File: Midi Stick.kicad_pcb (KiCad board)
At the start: 2 copper layers, 47.1 x 17.5 mm, 34 parts, among them J1 USB 2.0 Type A Plug, J2 Aux, J3 ICSP, Q1 Mosfet N, X1 X1E0000210019

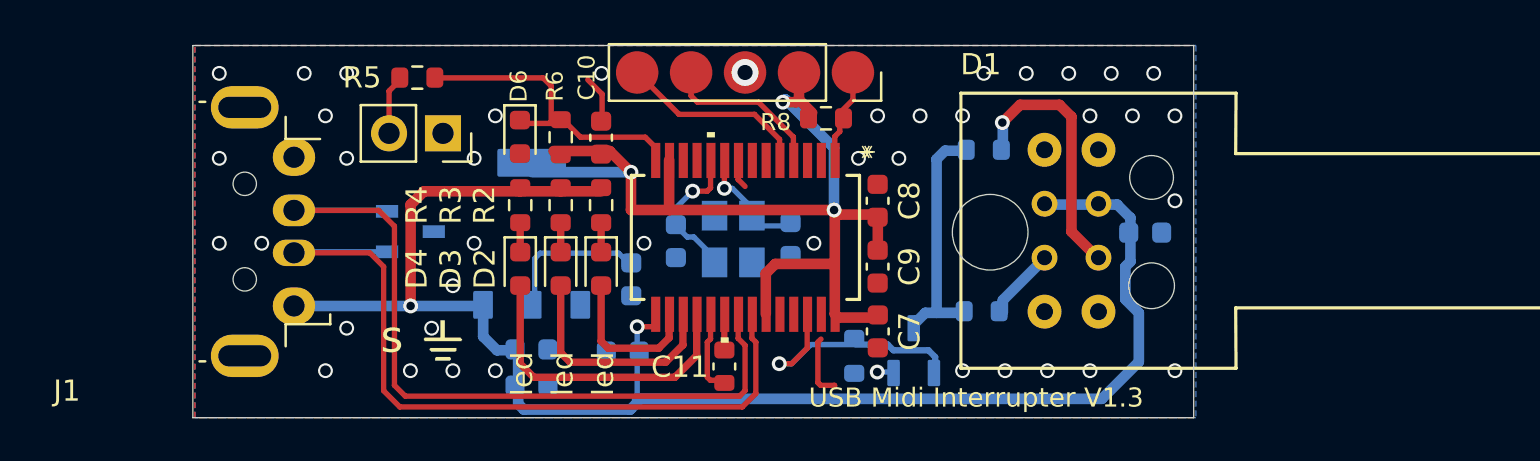
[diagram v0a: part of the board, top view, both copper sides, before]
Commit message: Fix recommended minimum PIC32 connection
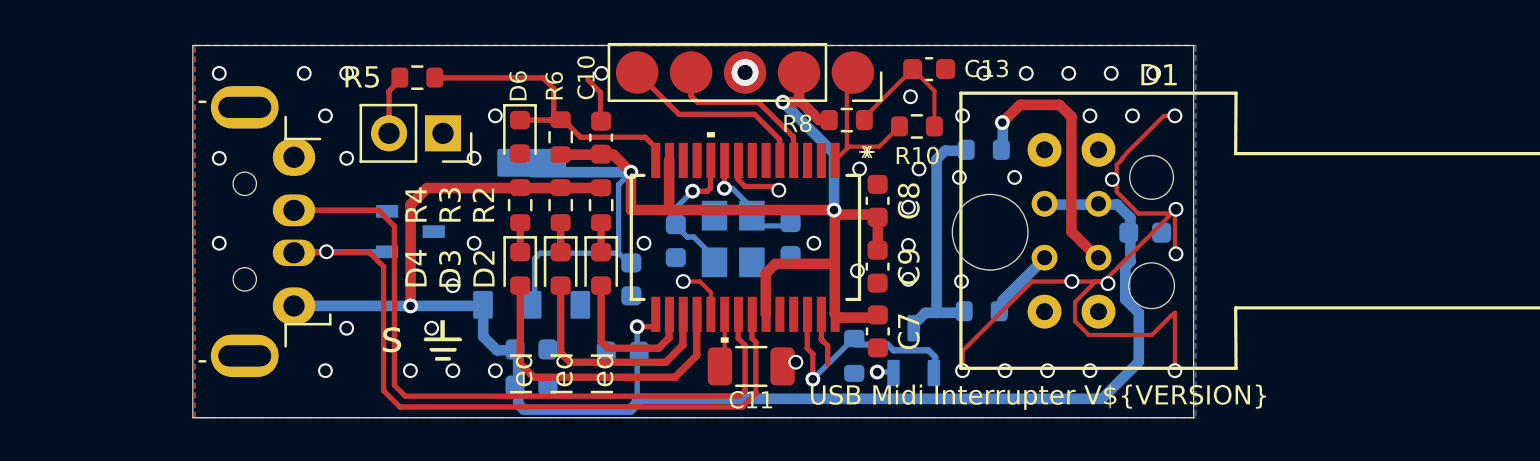
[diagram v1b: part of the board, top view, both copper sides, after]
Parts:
- added C13: 100nF, Capacitor_SMD:C_0603_1608Metric, F.Cu at (118.6, 54.9)
- added R10: 1k, Resistor_SMD:R_0603_1608Metric, F.Cu at (118.0, 57.6)
- C11: value 10uF -> 10uF / ESR≤3Ω (Tantalum); footprint Capacitor_SMD:C_0603_1608Metric -> Capacitor_SMD:C_1206_3216Metric
- moved C11 1.27 mm to (110.2, 68.9), turned to 180 degrees
- moved R8 0.99 mm to (114.7, 57.3)
- turned R9 to 0 degrees
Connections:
- net Net-(MCU1-VCore) renamed /VCAP
- R8 pad 2: /MCLR -> Net-(C13-Pad1)
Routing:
- net GND: track 11.4 -> 47.0 mm, vias 41 -> 54
- net Net-(D1-PadCE): track 0.00 -> 12.7 mm, vias 0 -> 1
- net (no net): track 11.2 -> 0.00 mm
- net Net-(C13-Pad1): track 0.00 -> 6.47 mm
- net +3.3V: track 54.6 -> 58.9 mm
- net /MCLR: track 4.86 -> 7.40 mm
- net /Out Sense: track 12.7 -> 11.2 mm, vias 1 -> 0
- net /Out: track 11.9 -> 10.6 mm
- net /VCAP: track 1.82 -> 2.55 mm
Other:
- board text added: "USB Midi Interrupter V${VERSION}"
- board text removed: "USB Midi Interrupter V1.3"

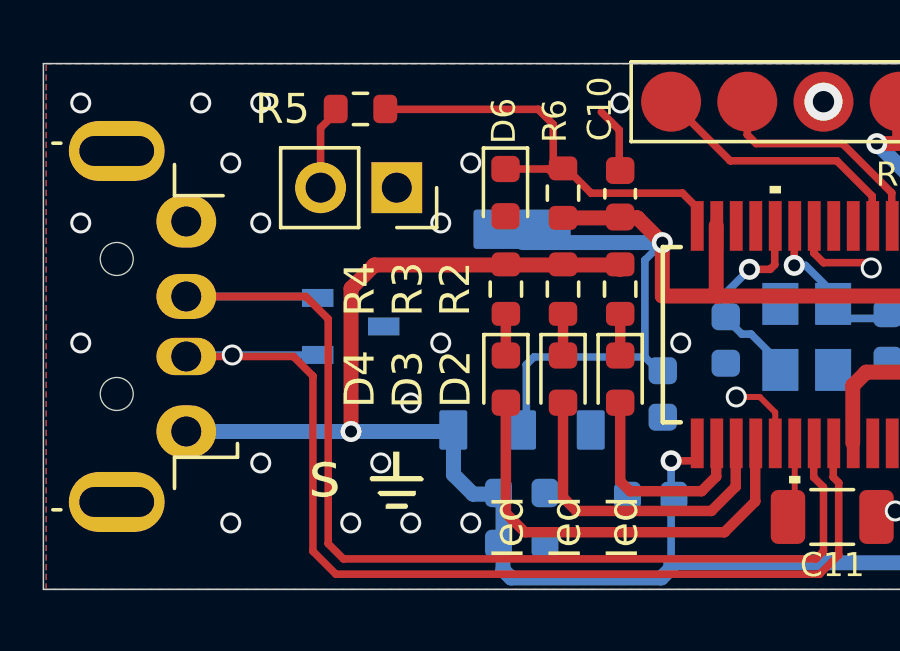
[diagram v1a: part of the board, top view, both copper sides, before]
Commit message: fix some labels
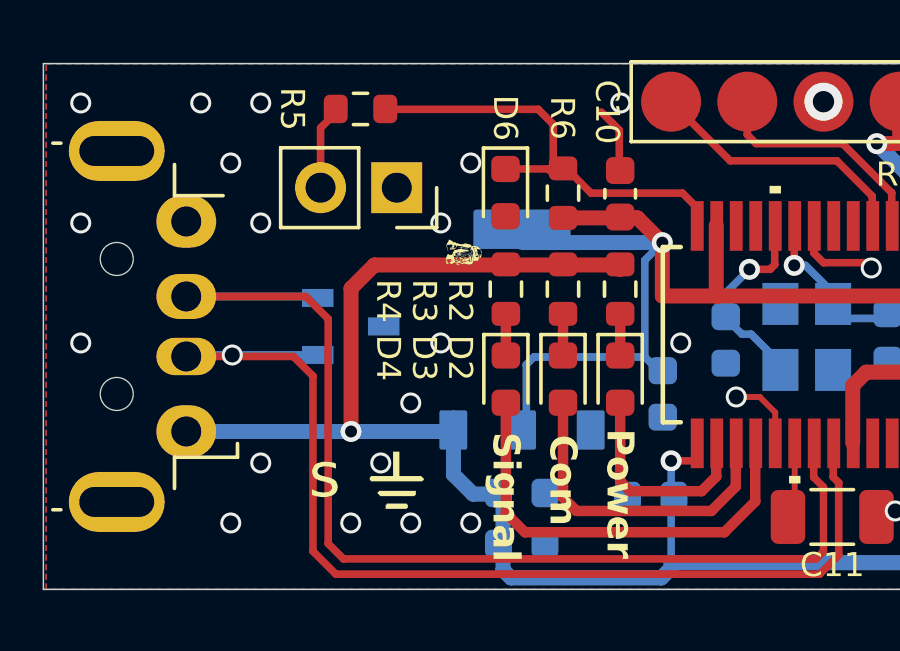
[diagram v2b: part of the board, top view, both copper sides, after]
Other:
- board text added: "Com"
- board text added: "Power"
- board text added: "Signal"
- board text removed: "led"

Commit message: WIP
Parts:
- removed the C1 at (112.0, 62.9)
- removed the C11 at (110.2, 68.9)
- removed the C12 at (104.1, 68.2)
- removed the C13 at (118.6, 54.9)
- removed the C2 at (106.6, 63.0)
- removed the C3 at (99.8, 68.1)
- removed the C4 at (99.8, 69.8)
- removed the C5 at (104.5, 64.8)
- removed the C7 at (116.1, 67.2)
- removed the C8 at (116.1, 61.1)
- removed the C9 at (116.1, 64.2)
- removed the J1 at (78.0, 62.5)
- removed MCU1: PIC32MX270F256B, Midi Stick:PIC32MX270F256B-I-SS_SSOP28_MC_MCH
- removed the R10 at (118.0, 57.6)
- removed the R8 at (114.7, 57.3)
- removed Reg1: 3.3V, Midi Stick:SOT229P700X180-4N
- removed X1: X1E0000210019, Midi Stick:CRYSTAL-SMD_4P-L3.2-W2.5-BL-1
- added C1: 10u, Capacitor_SMD:C_0805_2012Metric, F.Cu at (114.1, -1.65)
- added C1: 47u, Capacitor_SMD:C_0805_2012Metric, F.Cu at (48.2, 64.8)
- added C10: 4.7u, Capacitor_SMD:C_0402_1005Metric, F.Cu at (107.0, 28.7)
- added C10: 100n, Capacitor_SMD:C_0201_0603Metric, F.Cu at (35.1, 61.0)
- added C11: 100n, Capacitor_SMD:C_0402_1005Metric, F.Cu at (113.3, 21.3)
- added C11: 100n, Capacitor_SMD:C_0201_0603Metric, F.Cu at (31.4, 57.0)
- added C12: 100n, Capacitor_SMD:C_0402_1005Metric, F.Cu at (104.1, 14.5)
- added C12: 100n, Capacitor_SMD:C_0201_0603Metric, F.Cu at (31.1, 66.8)
- added C13: 100n, Capacitor_SMD:C_0402_1005Metric, F.Cu at (99.7, 18.5)
- added C13: 4u7, Capacitor_SMD:C_0402_1005Metric, F.Cu at (35.4, 67.4)
- added C14: 100n, Capacitor_SMD:C_0201_0603Metric, F.Cu at (26.1, 65.2)
- added C14: 10u, Capacitor_SMD:C_0805_2012Metric, F.Cu at (102.2, 90.0)
- added C14: 100n, Capacitor_SMD:C_0402_1005Metric, F.Cu at (113.3, 22.3)
- added C15: 100n, Capacitor_SMD:C_0201_0603Metric, F.Cu at (40.0, 57.0)
- added C15: 15p, Capacitor_SMD:C_0402_1005Metric, F.Cu at (93.8, 78.1)
- added C15: 100n, Capacitor_SMD:C_0402_1005Metric, F.Cu at (99.7, 23.3)
- added C16: 15p, Capacitor_SMD:C_0201_0603Metric, F.Cu at (23.1, 56.8)
- added C16: 100n, Capacitor_SMD:C_0402_1005Metric, F.Cu at (111.9, 25.9)
- added C16: 15p, Capacitor_SMD:C_0402_1005Metric, F.Cu at (94.0, 81.4)
- added C17: 15p, Capacitor_SMD:C_0201_0603Metric, F.Cu at (23.3, 61.4)
- added C17: 100n, Capacitor_SMD:C_0402_1005Metric, F.Cu at (112.7, 18.9)
- added C17: 100n, Capacitor_SMD:C_0402_1005Metric, F.Cu at (94.0, 83.4)
- added C18: 10u, Capacitor_SMD:C_0805_2012Metric, F.Cu at (102.2, 93.0)
- added C18: 4u7, Capacitor_SMD:C_0402_1005Metric, F.Cu at (34.1, 57.2)
- added C18: 100n, Capacitor_SMD:C_0402_1005Metric, F.Cu at (104.4, 27.9)
- added C19: 4u7, Capacitor_SMD:C_0402_1005Metric, F.Cu at (36.1, 64.0)
- added C19: 4.7u, RP2350_60QFN_minimal:C_0402_1005Metric_small_pads, F.Cu at (94.0, 85.4)
- added C19: 10u, Capacitor_SMD:C_0805_2012Metric, F.Cu at (91.3, -0.15)
- added C2: 100n, Capacitor_SMD:C_0402_1005Metric, F.Cu at (102.4, 4.68)
- added C2: 47u, Capacitor_SMD:C_0805_2012Metric, F.Cu at (43.2, 64.8)
- added C20: 4.7u, RP2350_60QFN_minimal:C_0402_1005Metric_small_pads, F.Cu at (98.4, 78.1)
- added C20: 4u7, Capacitor_SMD:C_0402_1005Metric, F.Cu at (35.1, 64.0)
- added C21: 4u7, Capacitor_SMD:C_0402_1005Metric, F.Cu at (35.4, 66.0)
- added C21: 100n, Capacitor_SMD:C_0402_1005Metric, F.Cu at (96.8, 81.4)
- added C22: 4.7u, Capacitor_SMD:C_0402_1005Metric, F.Cu at (96.8, 83.4)
- added C23: 4.7u, Capacitor_SMD:C_0402_1005Metric, F.Cu at (96.8, 85.4)
- added C24: 100n, Capacitor_SMD:C_0402_1005Metric, F.Cu at (106.7, 79.9)
- added C25: 100n, Capacitor_SMD:C_0402_1005Metric, F.Cu at (99.7, 81.4)
- added C26: 100n, Capacitor_SMD:C_0402_1005Metric, F.Cu at (99.7, 83.4)
- added C27: 100n, Capacitor_SMD:C_0402_1005Metric, F.Cu at (99.7, 85.4)
- added C28: 100n, Capacitor_SMD:C_0402_1005Metric, F.Cu at (103.4, 78.2)
- added C29: 100n, Capacitor_SMD:C_0402_1005Metric, F.Cu at (102.6, 81.4)
- added C3: 1n, Capacitor_SMD:C_0201_0603Metric, F.Cu at (35.7, 69.0)
- added C3: 15p, Capacitor_SMD:C_0402_1005Metric, F.Cu at (104.8, 30.9)
- added C30: 100n, Capacitor_SMD:C_0402_1005Metric, F.Cu at (102.6, 83.4)
- added C31: 100n, Capacitor_SMD:C_0402_1005Metric, F.Cu at (102.6, 85.4)
- added C32: 10u, Capacitor_SMD:C_0805_2012Metric, F.Cu at (102.2, 96.0)
- added C4: 100n, Capacitor_SMD:C_0201_0603Metric, F.Cu at (33.3, 57.4)
- added C4: 15p, Capacitor_SMD:C_0402_1005Metric, F.Cu at (107.8, 30.9)
- added C5: 100n, Capacitor_SMD:C_0201_0603Metric, F.Cu at (29.4, 57.4)
- added C5: 10u, Capacitor_SMD:C_0805_2012Metric, F.Cu at (115.2, 10.9)
- added C6: 4.7u, RP2350_60QFN_minimal:C_0402_1005Metric_small_pads, F.Cu at (108.2, 17.3)
- added C6: 100n, Capacitor_SMD:C_0201_0603Metric, F.Cu at (33.4, 66.4)
- added C7: 100n, Capacitor_SMD:C_0201_0603Metric, F.Cu at (30.5, 66.8)
- added C7: 4.7u, RP2350_60QFN_minimal:C_0402_1005Metric_small_pads, F.Cu at (108.2, 16.3)
- added C8: 100n, Capacitor_SMD:C_0402_1005Metric, F.Cu at (99.7, 20.9)
- added C8: 100n, Capacitor_SMD:C_0201_0603Metric, F.Cu at (26.1, 60.7)
- added C9: 4.7u, Capacitor_SMD:C_0402_1005Metric, F.Cu at (110.4, 16.8)
- added C9: 4u7, Capacitor_SMD:C_0201_0603Metric, F.Cu at (25.8, 61.9)
- added D1: PMEG6010ELR, Diode_SMD:D_SOD-123F, F.Cu at (50.0, 67.9)
- added D2: LTST-C191KGKT, LED_SMD:LED_0603_1608Metric, F.Cu at (51.8, 55.5)
- added D7: PMEG6010ELR, Diode_SMD:D_SOD-123F, F.Cu at (83.6, 106.2)
- added FID1: Fiducial, Fiducial:Fiducial_1mm_Mask2mm, F.Cu at (49.0, 56.1)
- added FID2: Fiducial, Fiducial:Fiducial_1mm_Mask2mm, F.Cu at (11.2, 67.1)
- added H1: MountingHole, MountingHole:MountingHole_2.7mm_M2.5, F.Cu at (92.2, -4.15)
- added H1: MountingHole, MountingHole:MountingHole_2.7mm_M2.5, F.Cu at (77.4, 81.9)
- added H2: MountingHole, MountingHole:MountingHole_2.7mm_M2.5, F.Cu at (77.4, 88.9)
- added H2: MountingHole, MountingHole:MountingHole_2.7mm_M2.5, F.Cu at (120.2, -4.15)
- added H3: MountingHole, MountingHole:MountingHole_2.7mm_M2.5, F.Cu at (77.4, 95.8)
- added H3: MountingHole, MountingHole:MountingHole_2.7mm_M2.5, F.Cu at (120.2, 39.0)
- added H4: MountingHole, MountingHole:MountingHole_2.7mm_M2.5, F.Cu at (92.2, 39.0)
- added H4: MountingHole, MountingHole:MountingHole_2.7mm_M2.5, F.Cu at (77.4, 102.8)
- added J1: USB_B_Micro, Connector_USB:USB_Micro-B_Amphenol_10103594-0001LF_Horizontal, F.Cu at (106.2, -5.31)
- added J1: ~, Pico 2 C:CON_PICO_1-20, F.Cu at (31.1, 53.0)
- added J2: Conn_02x18_Odd_Even, Connector_PinHeader_2.54mm:PinHeader_2x18_P2.54mm_Vertical, F.Cu at (82.1, -4.15)
- added J2: ~, Pico 2 C:CON_PICO_21-40, F.Cu at (31.1, 70.7)
- added J3: Conn_02x18_Odd_Even, Connector_PinHeader_2.54mm:PinHeader_2x18_P2.54mm_Vertical, F.Cu at (127.8, -4.15)
- added J3: USB_C_Receptacle_USB2.0_16P, Connector_USB:USB_C_Receptacle_GCT_USB4105-xx-A_16P_TopMnt_Horizontal, F.Cu at (55.6, 61.9)
- added J4: SM03B-SRSS-TB, Connector_JST:JST_SH_SM03B-SRSS-TB_1x03-1MP_P1.00mm_Horizontal, F.Cu at (8.93, 61.9)
- added J4: SM03B-SRSS-TB, Connector_JST:JST_SH_SM03B-SRSS-TB_1x03-1MP_P1.00mm_Horizontal, F.Cu at (113.8, 34.7)
- added J8: USB_C_Receptacle_USB2.0_16P, Connector_USB:USB_C_Receptacle_GCT_USB4105-xx-A_16P_TopMnt_Horizontal, F.Cu at (86.3, 62.5)
- added L1: 3.3u, RP2350_60QFN_minimal:L_pol_2016, F.Cu at (108.2, 14.7)
- added L1: SRN2512-2R2M, Inductor_SMD:L_1008_2520Metric, F.Cu at (45.7, 67.9)
- added L1: 3.3u, RP2350_60QFN_minimal:L_pol_2016, F.Cu at (82.6, 109.8)
- added L2: 3u3, Inductor_SMD:L_0603_1608Metric, F.Cu at (37.6, 64.0)
- added Q1: DMG1012T-7, Package_TO_SOT_SMD:SOT-523, F.Cu at (38.3, 68.3)
- added R1: 10k, Resistor_SMD:R_0201_0603Metric, F.Cu at (30.4, 68.5)
- added R1: DNF, Resistor_SMD:R_0402_1005Metric, F.Cu at (99.2, 4.05)
- added R10: 0, Resistor_SMD:R_0402_1005Metric, F.Cu at (95.1, 4.55)
- added R10: 5k6, Resistor_SMD:R_0201_0603Metric, F.Cu at (31.2, 68.5)
- added R10: 5k1, Resistor_SMD:R_0402_1005Metric, F.Cu at (92.6, 100.7)
- added R11: 1k, Resistor_SMD:R_0201_0603Metric, F.Cu at (37.7, 56.1)
- added R11: DNF, Resistor_SMD:R_0402_1005Metric, F.Cu at (92.6, 102.7)
- added R12: 27R, Resistor_SMD:R_0201_0603Metric, F.Cu at (36.6, 60.8)
- added R12: 0, Resistor_SMD:R_0402_1005Metric, F.Cu at (92.6, 104.7)
- added R13: DNF, Resistor_SMD:R_0402_1005Metric, F.Cu at (92.6, 106.7)
- added R13: 27R, Resistor_SMD:R_0201_0603Metric, F.Cu at (36.6, 61.5)
- added R14: 1k, Resistor_SMD:R_0201_0603Metric, F.Cu at (24.4, 61.4)
- added R14: 1k, Resistor_SMD:R_0402_1005Metric, F.Cu at (92.6, 108.7)
- added R16: 33, Resistor_SMD:R_0402_1005Metric, F.Cu at (95.6, 100.7)
- added R16: 100k, Resistor_SMD:R_0201_0603Metric, F.Cu at (35.7, 68.3)
- added R17: 33R, Resistor_SMD:R_0402_1005Metric, F.Cu at (37.1, 66.0)
- added R17: 1k, Resistor_SMD:R_0402_1005Metric, F.Cu at (95.6, 102.7)
- added R18: 100R, Resistor_SMD:R_0201_0603Metric, F.Cu at (24.5, 64.4)
- added R18: 27, Resistor_SMD:R_0402_1005Metric, F.Cu at (95.6, 104.7)
- added R19: 27, Resistor_SMD:R_0402_1005Metric, F.Cu at (95.6, 106.7)
- added R19: 100R, Resistor_SMD:R_0201_0603Metric, F.Cu at (24.1, 63.9)
- added R2: 100k, Resistor_SMD:R_0201_0603Metric, F.Cu at (49.7, 65.4)
- added R2: 1k, Resistor_SMD:R_0402_1005Metric, F.Cu at (105.8, 28.8)
- added R20: 5k1, Resistor_SMD:R_0402_1005Metric, B.Cu at (54.6, 65.1)
- added R21: 5k1, Resistor_SMD:R_0402_1005Metric, B.Cu at (54.6, 58.6)
- added R3: 470R, Resistor_SMD:R_0201_0603Metric, F.Cu at (49.4, 58.9)
- added R4: 1k, Resistor_SMD:R_0402_1005Metric, F.Cu at (121.6, 31.0)
- added R4: NO-FIT, Resistor_SMD:R_0201_0603Metric, F.Cu at (36.5, 56.1)
- added R5: 100k, Resistor_SMD:R_0201_0603Metric, F.Cu at (40.5, 69.0)
- added R5: 33, Resistor_SMD:R_0402_1005Metric, F.Cu at (110.4, 15.0)
- added R6: 1k, Resistor_SMD:R_0402_1005Metric, F.Cu at (95.1, 3.15)
- added R6: 100k, Resistor_SMD:R_0201_0603Metric, F.Cu at (40.5, 68.4)
- added R7: 27, Resistor_SMD:R_0402_1005Metric, F.Cu at (105.1, 14.5)
- added R7: 200R, Resistor_SMD:R_0402_1005Metric, F.Cu at (42.4, 67.4)
- added R8: 100k, Resistor_SMD:R_0201_0603Metric, F.Cu at (50.2, 58.9)
- added R8: 27, Resistor_SMD:R_0402_1005Metric, F.Cu at (106.1, 14.5)
- added R8: 5k1, Resistor_SMD:R_0402_1005Metric, F.Cu at (92.6, 98.7)
- added R9: 1R, Resistor_SMD:R_0201_0603Metric, F.Cu at (40.5, 67.7)
- added R9: DNF, Resistor_SMD:R_0402_1005Metric, F.Cu at (97.5, 4.05)
- added SW1: SW_Push, Button_Switch_SMD:SW_Push_1P1T_NO_Vertical_Wuerth_434133025816, F.Cu at (97.4, -2.95)
- added SW1: SW_Push, Button_Switch_SMD:SW_Push_1P1T_NO_Vertical_Wuerth_434133025816, F.Cu at (87.9, 55.3)
- added SW1: PTS810 SJK 250 SMTR LFS, Button_Switch_SMD:SW_SPST_PTS810, F.Cu at (44.6, 58.4)
- added SW2: SW_Push, Button_Switch_SMD:SW_Push_1P1T_NO_Vertical_Wuerth_434133025816, F.Cu at (118.0, 29.3)
- added TP1: TestPoint, TestPoint:TestPoint_Pad_1.5x1.5mm, B.Cu at (52.1, 61.9)
- added TP10: TestPoint, TestPoint:TestPoint_Pad_1.5x1.5mm, B.Cu at (7.08, 64.4)
- added TP2: TestPoint, TestPoint:TestPoint_Pad_1.5x1.5mm, B.Cu at (55.4, 62.9)
- added TP3: TestPoint, TestPoint:TestPoint_Pad_1.5x1.5mm, B.Cu at (55.4, 60.9)
- added TP4: TestPoint, TestPoint:TestPoint_Pad_1.5x1.5mm, B.Cu at (48.6, 59.4)
- added TP5: TestPoint, TestPoint:TestPoint_Pad_1.5x1.5mm, B.Cu at (46.1, 59.4)
- added TP6: TestPoint, TestPoint:TestPoint_Pad_1.5x1.5mm, B.Cu at (43.6, 59.4)
- added TP7: TestPoint, TestPoint:TestPoint_Pad_1.5x1.5mm, B.Cu at (36.1, 62.9)
- added TP8: TestPoint, TestPoint:TestPoint_Pad_1.5x1.5mm, B.Cu at (7.08, 59.5)
- added TP9: TestPoint, TestPoint:TestPoint_Pad_1.5x1.5mm, B.Cu at (7.08, 62.0)
- added U1: W25Q128JVS, Package_SO:SOIC-8_5.23x5.23mm_P1.27mm, F.Cu at (112.5, 68.0)
- added U1: RP2350_60QFN, Pico 2 C:RP2350-QFN-60-1EP_7x7_P0.4mm_EP3.4x3.4mm_ThermalVias, F.Cu at (30.7, 61.9)
- added U1: RP2350_60QFN, RP2350_60QFN_minimal:RP2350-QFN-60-1EP_7x7_P0.4mm_EP3.4x3.4mm_ThermalVias, F.Cu at (106.2, 21.9)
- added U2: RT6150B-33GQW, Package_DFN_QFN:DFN-10-1EP_2.6x2.6mm_P0.5mm_EP1.3x2.2mm, F.Cu at (45.7, 64.8)
- added U2: NCP1117-3.3_SOT223, Package_TO_SOT_SMD:SOT-223-3_TabPin2, F.Cu at (114.2, 4.70)
- added U2: NCP1117-3.3_SOT223, Package_TO_SOT_SMD:SOT-223-3_TabPin2, B.Cu at (100.7, 65.1)
- added U3: W25Q32RVXHJQ TR, Package_DFN_QFN:TDFN-8-1EP_3x2mm_P0.5mm_EP1.3x1.4mm, F.Cu at (37.5, 57.7)
- added U3: RP2350_60QFN, RP2350_60QFN_minimal:RP2350-QFN-60-1EP_7x7_P0.4mm_EP3.4x3.4mm_ThermalVias, F.Cu at (112.0, 60.9)
- added U3: W25Q128JVS, Package_SO:SOIC-8_5.23x5.23mm_P1.27mm, F.Cu at (99.2, 9.13)
- added Y1: ECS-120-8-33-JGN-TR, Crystal:Crystal_SMD_SeikoEpson_FA238-4Pin_3.2x2.5mm, F.Cu at (23.6, 59.1)
- added Y1: ABM8-272-T3, Crystal:Crystal_SMD_3225-4Pin_3.2x2.5mm, F.Cu at (106.2, 34.3)
- added Y1: ABM8-272-T3, Crystal:Crystal_SMD_3225-4Pin_3.2x2.5mm, B.Cu at (108.8, 60.0)
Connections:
- net +5V renamed VBUS
- D5 pad 1: /D- -> /USB_D-
- D5 pad 2: /D+ -> /USB_D+
- J3 pad 1: /MCLR -> /SWCLK
- J3 pad 2: +3.3V -> GND
- J3 pad 3: GND -> /SWD
- J3 pad 4: /PGD -> GND
- J3 pad 5: /PGC -> +3V3
- R6 pad 2: +3.3V -> +3V3
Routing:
- net (no net): track 0.00 -> 1818.4 mm, vias 0 -> 47
- net +3.3V: track 58.9 -> 2.48 mm, vias 3 -> 0
- net +3V3: track 0.00 -> 50.6 mm
- net GND: track 47.0 -> 84.8 mm, vias 54 -> 136
- net /D+: track 37.0 -> 0.00 mm
- net /D-: track 36.1 -> 0.00 mm, vias 1 -> 0
- net VBUS: track 76.2 -> 44.2 mm, vias 2 -> 0
- net /PGC: track 9.36 -> 0.00 mm
- net /PGD: track 8.18 -> 0.00 mm
- net /MCLR: track 7.40 -> 0.00 mm
- net Net-(MCU1-RA3_/_CLKO): track 6.88 -> 0.00 mm, vias 1 -> 0
- net Net-(C13-Pad1): track 6.47 -> 0.00 mm
- net Net-(MCU1-RA2_/_CLKI): track 5.92 -> 0.00 mm, vias 1 -> 0
- net /Aux: track 15.2 -> 10.8 mm
- net /Power LED: track 7.42 -> 3.22 mm
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- added copper zone on B.Cu, net (none)
- added copper zone on F.Cu, net (none)
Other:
- board size 47.1 x 17.5 mm -> 126.6 x 80.5 mm
- board text added: "2"
- board text added: "3V3"
- board text added: "ADC 26-29"
- board text added: "BOOTSEL"
- board text added: "CLK"
- board text added: "DEBUG"
- board text added: "DIO"
- board text added: "GND"
- board text added: "GP0"
- board text added: "GP1"
- board text added: "GP10"
- board text added: "GP11"
- board text added: "GP12"
- board text added: "GP13"
- board text added: "GP14"
- board text added: "GP15"
- board text added: "GP16"
- board text added: "GP17"
- board text added: "GP18"
- board text added: "GP19"
- board text added: "GP2"
- board text added: "GP20"
- board text added: "GP21"
- board text added: "GP22"
- board text added: "GP23"
- board text added: "GP24"
- board text added: "GP25"
- board text added: "GP26"
- board text added: "GP27"
- board text added: "GP28"
- board text added: "GP29"
- board text added: "GP3"
- board text added: "GP4"
- board text added: "GP5"
- board text added: "GP6"
- board text added: "GP7"
- board text added: "GP8"
- board text added: "GP9"
- board text added: "LED"
- board text added: "Minimal Design Example REV3"
- board text added: "Outer Row GND"
- board text added: "RUN"
- board text added: "Raspberry Pi RP2350A QFN-60"
- board text added: "SWCLK"
- board text added: "SWD"
- board text added: "USB"
- board text added: "project piCo"
- board text added: "v1 by CS"

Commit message: WIP
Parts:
- removed C1, C5: 10u, Capacitor_SMD:C_0805_2012Metric
- removed C1, C2: 47u, Capacitor_SMD:C_0805_2012Metric
- removed the C10 at (107.0, 28.7)
- removed the C10 at (35.1, 61.0)
- removed C11, C12, C13, C2, C8: 100n, Capacitor_SMD:C_0402_1005Metric
- removed C11, C12, C4, C5, C7, C8: 100n, Capacitor_SMD:C_0201_0603Metric
- removed C13: 4u7, Capacitor_SMD:C_0402_1005Metric
- removed the C14 at (26.1, 65.2)
- removed the C14 at (113.3, 22.3)
- removed the C15 at (40.0, 57.0)
- removed the C15 at (99.7, 23.3)
- removed the C16 at (23.1, 56.8)
- removed the C16 at (111.9, 25.9)
- removed the C17 at (23.3, 61.4)
- removed the C17 at (112.7, 18.9)
- removed the C18 at (34.1, 57.2)
- removed the C18 at (104.4, 27.9)
- removed the C19 at (36.1, 64.0)
- removed the C19 at (91.3, -0.15)
- removed the C20 at (35.1, 64.0)
- removed the C21 at (35.4, 66.0)
- removed C3: 1n, Capacitor_SMD:C_0201_0603Metric
- removed C3, C4: 15p, Capacitor_SMD:C_0402_1005Metric
- removed the C6 at (108.2, 17.3)
- removed the C6 at (33.4, 66.4)
- removed C7: 4.7u, RP2350_60QFN_minimal:C_0402_1005Metric_small_pads
- removed C9: 4.7u, Capacitor_SMD:C_0402_1005Metric
- removed C9: 4u7, Capacitor_SMD:C_0201_0603Metric
- removed the D1 at (50.0, 67.9)
- removed the D2 at (51.8, 55.5)
- removed FID1, FID2: Fiducial, Fiducial:Fiducial_1mm_Mask2mm
- removed H1 (x2), H2 (x2), H3 (x2), H4 (x2): MountingHole, MountingHole:MountingHole_2.7mm_M2.5
- removed J1: USB_B_Micro, Connector_USB:USB_Micro-B_Amphenol_10103594-0001LF_Horizontal
- removed J1: ~, Pico 2 C:CON_PICO_1-20
- removed the J2 at (82.1, -4.15)
- removed the J2 at (31.1, 70.7)
- removed the J3 at (127.8, -4.15)
- removed the J3 at (55.6, 61.9)
- removed J4 (x2): SM03B-SRSS-TB, Connector_JST:JST_SH_SM03B-SRSS-TB_1x03-1MP_P1.00mm_Horizontal
- removed the L1 at (108.2, 14.7)
- removed the L1 at (45.7, 67.9)
- removed L2: 3u3, Inductor_SMD:L_0603_1608Metric
- removed the Q1 at (38.3, 68.3)
- removed the R1 at (30.4, 68.5)
- removed the R1 at (99.2, 4.05)
- removed the R10 at (95.1, 4.55)
- removed the R10 at (31.2, 68.5)
- removed the R11 at (37.7, 56.1)
- removed the R12 at (36.6, 60.8)
- removed the R13 at (36.6, 61.5)
- removed the R14 at (24.4, 61.4)
- removed the R16 at (35.7, 68.3)
- removed the R17 at (37.1, 66.0)
- removed the R18 at (24.5, 64.4)
- removed the R19 at (24.1, 63.9)
- removed the R2 at (49.7, 65.4)
- removed the R2 at (105.8, 28.8)
- removed R20, R21: 5k1, Resistor_SMD:R_0402_1005Metric
- removed the R3 at (49.4, 58.9)
- removed the R4 at (121.6, 31.0)
- removed the R4 at (36.5, 56.1)
- removed the R5 at (40.5, 69.0)
- removed the R5 at (110.4, 15.0)
- removed the R6 at (95.1, 3.15)
- removed the R6 at (40.5, 68.4)
- removed the R7 at (105.1, 14.5)
- removed the R7 at (42.4, 67.4)
- removed the R8 at (50.2, 58.9)
- removed the R8 at (106.1, 14.5)
- removed the R9 at (40.5, 67.7)
- removed the R9 at (97.5, 4.05)
- removed the SW1 at (97.4, -2.95)
- removed the SW1 at (44.6, 58.4)
- removed SW2: SW_Push, Button_Switch_SMD:SW_Push_1P1T_NO_Vertical_Wuerth_434133025816
- removed TP1, TP10, TP2, TP3, TP4, TP5, TP6, TP7, TP8, TP9: TestPoint, TestPoint:TestPoint_Pad_1.5x1.5mm
- removed the U1 at (30.7, 61.9)
- removed the U1 at (106.2, 21.9)
- removed the U2 at (45.7, 64.8)
- removed the U2 at (114.2, 4.70)
- removed the U3 at (37.5, 57.7)
- removed the U3 at (99.2, 9.13)
- removed the Y1 at (23.6, 59.1)
- removed the Y1 at (106.2, 34.3)
- C15, C16, C17, C25, C26, C27, C29, C30, C31, D7, L1, R10, R14, R17, R18, R19, R8: moved to B.Cu
- C19: footprint RP2350_60QFN_minimal:C_0402_1005Metric_small_pads -> Capacitor_SMD:C_0402_1005Metric; moved to B.Cu
- C20: footprint RP2350_60QFN_minimal:C_0402_1005Metric_small_pads -> Capacitor_SMD:C_0402_1005Metric
- moved L1 50.5 mm to (108.2, 66.3)
- moved R13 48.3 mm to (118.9, 66.2)
- moved R14 47.9 mm to (107.9, 63.3), turned to 180 degrees
- moved R17 47.2 mm to (92.0, 55.7), turned to 180 degrees
- moved R12 44.9 mm to (118.8, 68.2)
- moved R19 43.2 mm to (110.8, 66.3), turned to 90 degrees
- moved R18 41.9 mm to (112.1, 66.3), turned to 90 degrees
- moved R11 41.5 mm to (118.0, 69.9), turned to 180 degrees
- moved C18 39.9 mm to (118.5, 56.6), turned to 90 degrees
- moved D7 39.3 mm to (94.0, 68.3), turned to 180 degrees
- moved R8 39.1 mm to (87.6, 60.0), turned to 90 degrees
- moved C32 39.0 mm to (117.3, 60.0), turned to -90 degrees
- moved R16 38.7 mm to (107.4, 63.9), turned to -90 degrees
- moved R10 36.4 mm to (87.6, 64.7), turned to -90 degrees
- moved C14 30.6 mm to (117.3, 63.4), turned to -90 degrees
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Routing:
- net (no net): track 1818.4 -> 0.00 mm, vias 47 -> 0
- net +3V3: track 50.6 -> 0.38 mm
- net GND: track 84.8 -> 37.6 mm, vias 136 -> 25
- net /USB_D-: track 1.13 -> 8.29 mm
- net /USB_D+: track 1.52 -> 5.30 mm, vias 0 -> 1
- net Net-(J8-CC1): track 0.00 -> 2.99 mm, vias 0 -> 1
- net Net-(J8-CC2): track 0.00 -> 2.41 mm, vias 0 -> 1
- net /Signal LED: track 11.4 -> 9.66 mm
- net /Com LED: track 8.43 -> 7.06 mm
- net /Out: track 7.38 -> 6.37 mm
- removed copper zone on B.Cu, net (none)
- removed copper zone on F.Cu, net (none)
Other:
- board size 126.6 x 80.5 mm -> 47.1 x 17.5 mm
- board text removed: "2"
- board text removed: "3V3"
- board text removed: "ADC 26-29"
- board text removed: "BOOTSEL"
- board text removed: "CLK"
- board text removed: "DEBUG"
- board text removed: "DIO"
- board text removed: "GND"
- board text removed: "GP0"
- board text removed: "GP1"
- board text removed: "GP10"
- board text removed: "GP11"
- board text removed: "GP12"
- board text removed: "GP13"
- board text removed: "GP14"
- board text removed: "GP15"
- board text removed: "GP16"
- board text removed: "GP17"
- board text removed: "GP18"
- board text removed: "GP19"
- board text removed: "GP2"
- board text removed: "GP20"
- board text removed: "GP21"
- board text removed: "GP22"
- board text removed: "GP23"
- board text removed: "GP24"
- board text removed: "GP25"
- board text removed: "GP26"
- board text removed: "GP27"
- board text removed: "GP28"
- board text removed: "GP29"
- board text removed: "GP3"
- board text removed: "GP4"
- board text removed: "GP5"
- board text removed: "GP6"
- board text removed: "GP7"
- board text removed: "GP8"
- board text removed: "GP9"
- board text removed: "LED"
- board text removed: "Minimal Design Example REV3"
- board text removed: "Outer Row GND"
- board text removed: "RUN"
- board text removed: "Raspberry Pi RP2350A QFN-60"
- board text removed: "SWCLK"
- board text removed: "SWD"
- board text removed: "USB"
- board text removed: "project piCo"
- board text removed: "v1 by CS"
